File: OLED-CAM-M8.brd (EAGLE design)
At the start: 87.6 x 61 mm, 17 parts, among them J5 U.FL

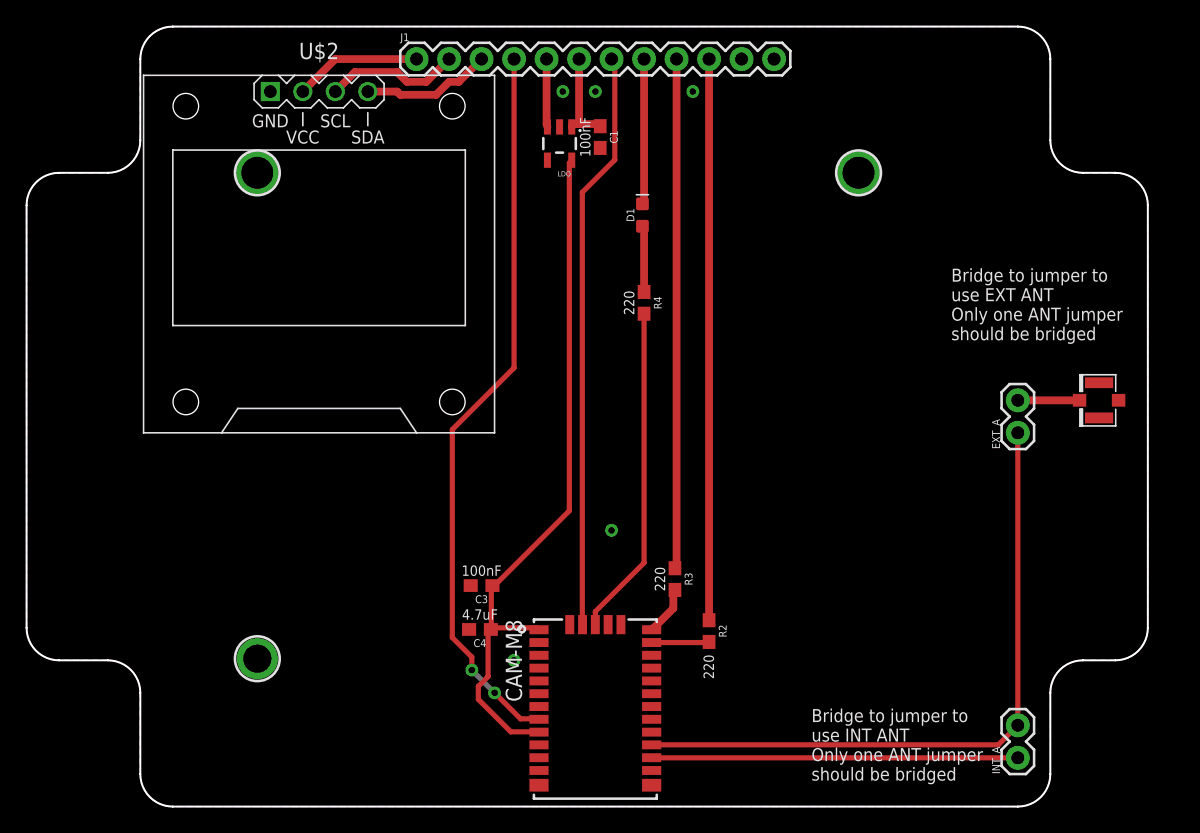
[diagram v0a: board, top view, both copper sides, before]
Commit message: Added GND vias and notes
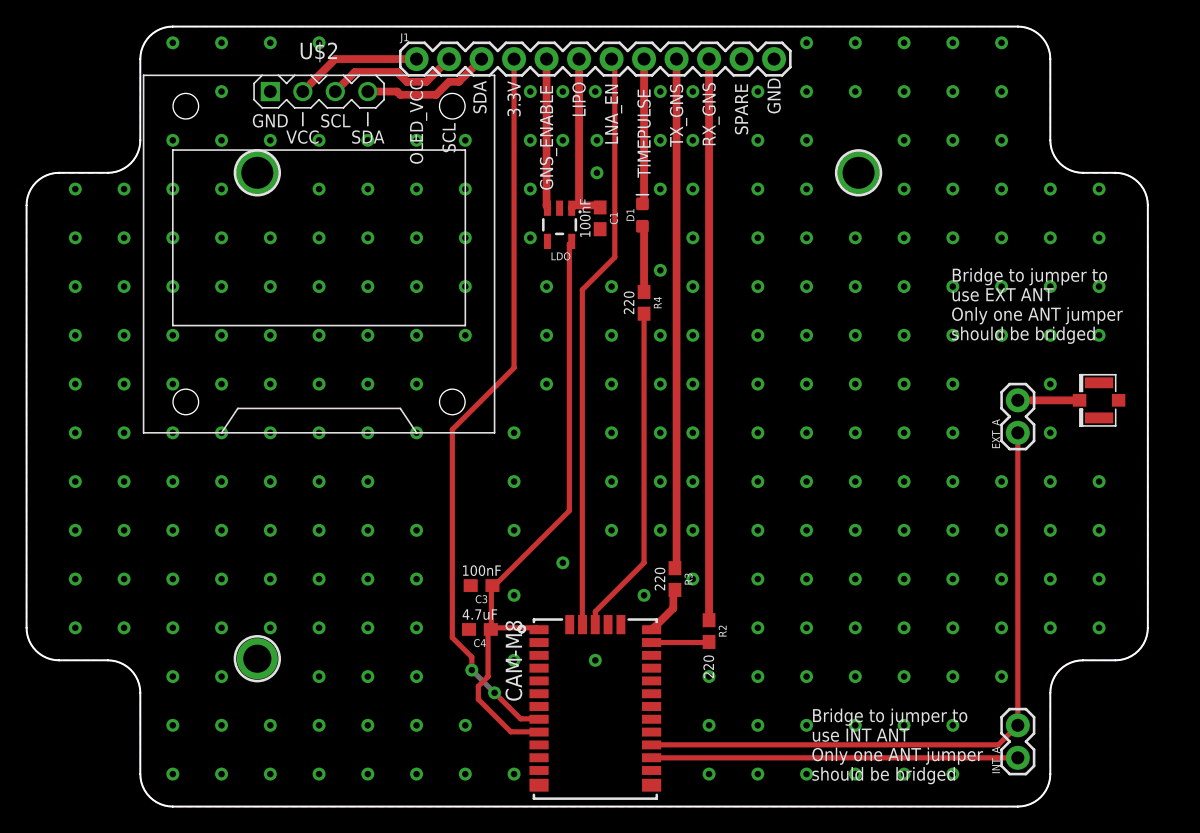
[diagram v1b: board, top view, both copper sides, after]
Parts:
- moved C1 6.35 mm to (44.8, 46.0)
- moved LDO 6.35 mm to (41.7, 45.5)
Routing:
- net GNS_VCC: track 54.9 -> 48.6 mm
- net LIPO: track 7.55 -> 13.9 mm
- net GNS_ENABLE: track 5.31 -> 11.7 mm
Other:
- board text added: "3.3V"
- board text added: "GND"
- board text added: "GNS_ENABLE"
- board text added: "LIPO"
- board text added: "LNA_EN"
- board text added: "OLED_VCC"
- board text added: "RX_GNS"
- board text added: "SCL"
- board text added: "SDA"
- board text added: "SPARE"
- board text added: "TIMEPULSE"
- board text added: "TX_GNS"

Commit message: Added mounting hole
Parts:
- added U$1: MOUNTINGHOLE2.0, microbuilder:MOUNTINGHOLE_2.0_PLATED
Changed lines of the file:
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@@
 <attribute name="VALUE" x="29.21" y="56.388" size="0.6096" layer="27" font="vector" ratio="20"/>
 </element>
+<element name="U$1" library="microbuilder" package="MOUNTINGHOLE_2.0_PLATED" value="MOUNTINGHOLE2.0" x="65.024" y="11.557" smashed="yes"/>
 </elements>
 <signals>
@@
 <via x="60.96" y="13.97" extent="1-16" drill="0.508"/>
 <via x="60.96" y="10.16" extent="1-16" drill="0.508"/>
-<via x="64.77" y="10.16" extent="1-16" drill="0.508"/>
-<via x="64.77" y="13.97" extent="1-16" drill="0.508"/>
 <via x="68.58" y="13.97" extent="1-16" drill="0.508"/>
 <via x="68.58" y="10.16" extent="1-16" drill="0.508"/>

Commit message: Swapped VCC GND
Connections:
- net GND: now also U$2.2; no longer U$2.1
- net OLED_VCC: now also U$2.1; no longer U$2.2
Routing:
- net OLED_VCC: track 9.94 -> 13.4 mm
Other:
- board text added: "v0.4 gregcope@gmail.com OLED-CAM-M8"
- board text removed: "v0.2 gregcope@gmail.com OLED-CAM-M8"
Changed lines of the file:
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@@
 <board>
 <plain>
-<text x="51.181" y="20.447" size="1.778" layer="26">v0.2
+<text x="51.181" y="20.447" size="1.778" layer="26">v0.4
 gregcope@gmail.com
 OLED-CAM-M8</text>
@@
 <contactref element="J5" pad="2"/>
 <contactref element="J5" pad="1"/>
-<contactref element="U$2" pad="1"/>
 <contactref element="J1" pad="12"/>
 <via x="38.1" y="11.43" extent="1-16" drill="0.508"/>
@@
 <via x="76.2" y="55.88" extent="1-16" drill="0.508"/>
 <via x="15.24" y="59.69" extent="1-16" drill="0.508"/>
-<via x="19.05" y="59.69" extent="1-16" drill="0.508"/>
 <via x="11.43" y="59.69" extent="1-16" drill="0.508"/>
 <via x="57.15" y="48.26" extent="1-16" drill="0.508"/>
@@
 <via x="76.2" y="52.07" extent="1-16" drill="0.508"/>
 <via x="76.2" y="48.26" extent="1-16" drill="0.508"/>
-<via x="22.86" y="59.69" extent="1-16" drill="0.508"/>
 <via x="80.01" y="48.26" extent="1-16" drill="0.508"/>
 <via x="52.07" y="55.88" extent="1-16" drill="0.508"/>
@@
 <via x="80.01" y="44.45" extent="1-16" drill="0.508"/>
 <via x="80.01" y="40.64" extent="1-16" drill="0.508"/>
+<contactref element="U$2" pad="2"/>
+<via x="19.05" y="59.69" extent="1-16" drill="0.508"/>
+<via x="22.86" y="59.69" extent="1-16" drill="0.508"/>
+<via x="26.67" y="59.69" extent="1-16" drill="0.508"/>
 </signal>
 <signal name="3.3V" class="2">
@@
 <signal name="OLED_VCC">
 <contactref element="J1" pad="1"/>
-<contactref element="U$2" pad="2"/>
-<wire x1="24.13" y1="58.42" x2="21.59" y2="55.88" width="0.6096" layer="1"/>
-<wire x1="30.48" y1="58.42" x2="24.13" y2="58.42" width="0.6096" layer="1"/>
+<contactref element="U$2" pad="1"/>
+<wire x1="19.05" y1="57.404" x2="19.05" y2="55.88" width="0.6096" layer="16"/>
+<wire x1="19.812" y1="58.166" x2="19.05" y2="57.404" width="0.6096" layer="16"/>
+<wire x1="28.702" y1="58.166" x2="19.812" y2="58.166" width="0.6096" layer="16"/>
+<wire x1="28.956" y1="58.42" x2="28.702" y2="58.166" width="0.6096" layer="16"/>
+<wire x1="30.48" y1="58.42" x2="28.956" y2="58.42" width="0.6096" layer="16"/>
 </signal>
 <signal name="SCL">

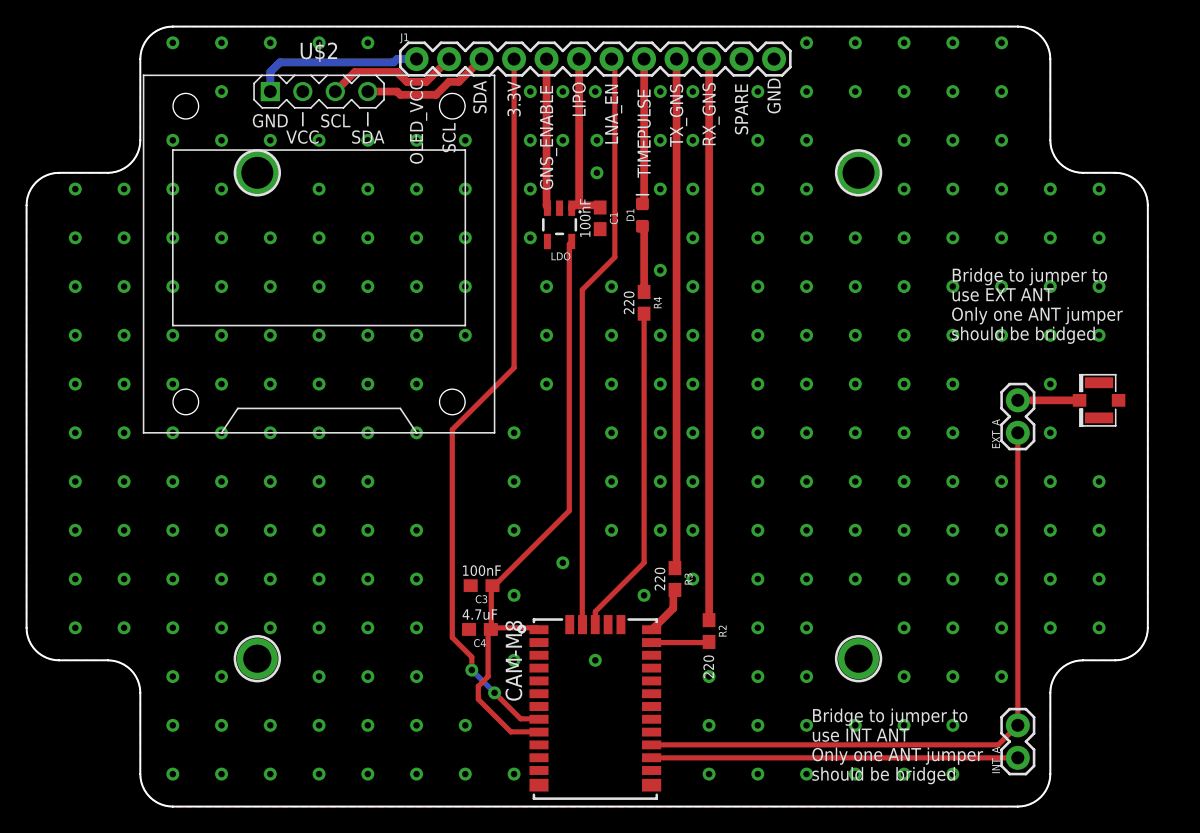
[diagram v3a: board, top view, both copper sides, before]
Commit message: removed mounting hole and moved 100n cap
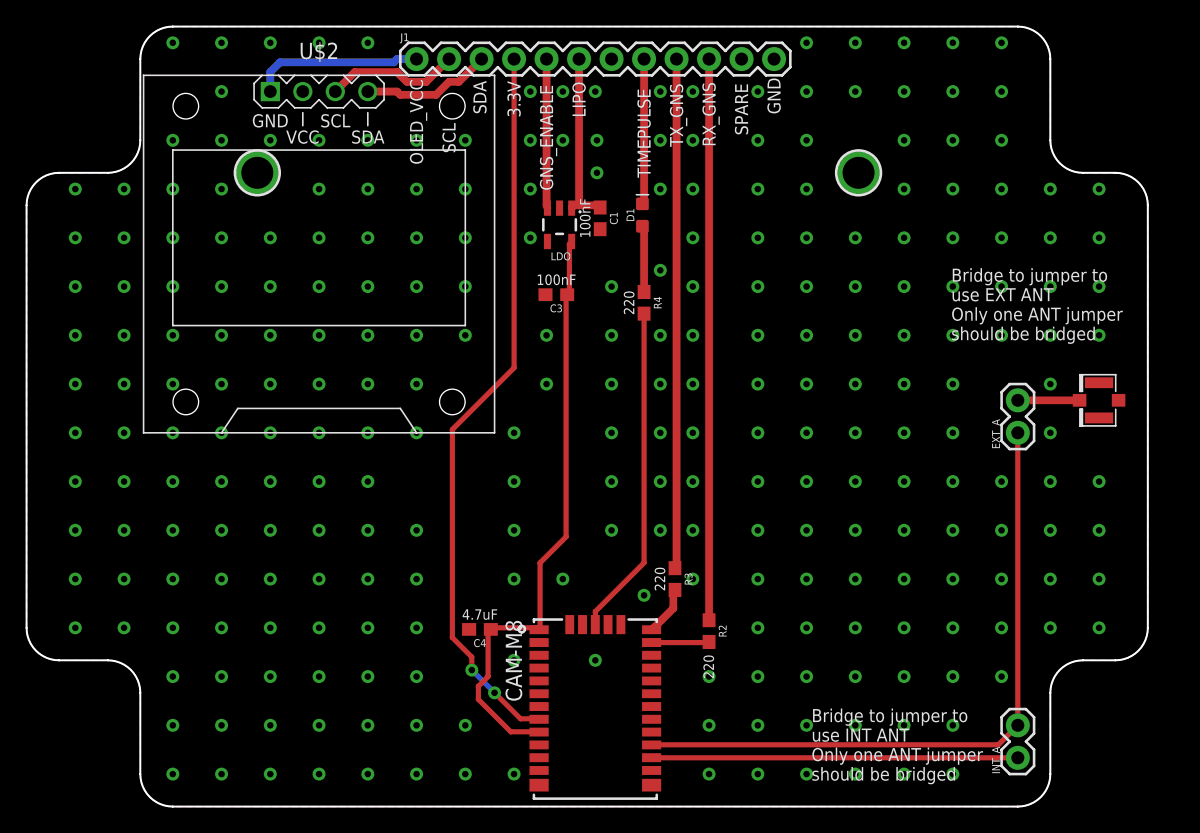
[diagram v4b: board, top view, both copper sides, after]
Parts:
- removed U$1, U$9: MOUNTINGHOLE2.0, microbuilder:MOUNTINGHOLE_2.0_PLATED
- moved C3 23.5 mm to (41.4, 40.0)
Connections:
- removed net LNA_EN: J1.7, U$5.30
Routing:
- net LNA_EN: track 45.4 -> 0.00 mm
- net GNS_VCC: track 48.6 -> 47.3 mm
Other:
- board text removed: "LNA_EN"
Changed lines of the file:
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@@
 <text x="51.308" y="51.562" size="1.016" layer="25" font="vector" ratio="20" rot="R90">TX_GNS</text>
 <text x="48.768" y="49.149" size="1.016" layer="25" font="vector" ratio="20" rot="R90">TIMEPULSE</text>
-<text x="46.228" y="51.689" size="1.016" layer="25" font="vector" ratio="20" rot="R90">LNA_EN</text>
 <text x="43.688" y="53.848" size="1.016" layer="25" font="vector" ratio="20" rot="R90">LIPO</text>
 <text x="41.148" y="48.133" size="1.016" layer="25" font="vector" ratio="20" rot="R90">GNS_ENABLE</text>
@@
 <attribute name="VALUE" x="44.069" y="45.974" size="0.8128" layer="25" font="vector" ratio="20" rot="R270" align="top-center"/>
 </element>
-<element name="C3" library="SparkFun-Capacitors" library_urn="urn:adsk.eagle:library:510" package="0603" package3d_urn="urn:adsk.eagle:package:37414/1" value="100nF" x="35.56" y="17.272" smashed="yes" rot="R180">
-<attribute name="NAME" x="35.56" y="16.51" size="0.6096" layer="25" font="vector" ratio="20" rot="R180" align="bottom-center"/>
-<attribute name="PROD_ID" value="CAP-08604" x="66.04" y="21.082" size="1.778" layer="27" rot="R180" display="off"/>
-<attribute name="VALUE" x="35.56" y="18.034" size="0.8128" layer="25" font="vector" ratio="20" rot="R180" align="top-center"/>
+<element name="C3" library="SparkFun-Capacitors" library_urn="urn:adsk.eagle:library:510" package="0603" package3d_urn="urn:adsk.eagle:package:37414/1" value="100nF" x="41.402" y="40.005" smashed="yes" rot="R180">
+<attribute name="NAME" x="41.402" y="39.243" size="0.6096" layer="25" font="vector" ratio="20" rot="R180" align="bottom-center"/>
+<attribute name="PROD_ID" value="CAP-08604" x="71.882" y="43.815" size="1.778" layer="27" rot="R180" display="off"/>
+<attribute name="VALUE" x="41.402" y="40.767" size="0.8128" layer="25" font="vector" ratio="20" rot="R180" align="top-center"/>
 </element>
 <element name="R2" library="SparkFun-Resistors" library_urn="urn:adsk.eagle:library:532" package="0603" package3d_urn="urn:adsk.eagle:package:39650/1" value="220" x="53.34" y="13.716" smashed="yes" rot="R270">
@@
 <attribute name="VALUE" x="48.768" y="46.228" size="0.6096" layer="27" font="vector" ratio="20" rot="R90" align="top-center"/>
 </element>
-<element name="U$9" library="microbuilder" package="MOUNTINGHOLE_2.0_PLATED" value="MOUNTINGHOLE2.0" x="18.034" y="11.557" smashed="yes"/>
 <element name="J5" library="SparkFun-Connectors" library_urn="urn:adsk.eagle:library:513" package="U.FL" package3d_urn="urn:adsk.eagle:package:38237/1" value="U.FL" x="83.82" y="31.75" smashed="yes" rot="R180">
 <attribute name="PROD_ID" value="CONN-09193" x="83.82" y="31.75" size="1.778" layer="27" rot="R180" display="off"/>
@@
 <attribute name="VALUE" x="29.21" y="56.388" size="0.6096" layer="27" font="vector" ratio="20"/>
 </element>
-<element name="U$1" library="microbuilder" package="MOUNTINGHOLE_2.0_PLATED" value="MOUNTINGHOLE2.0" x="65.024" y="11.557" smashed="yes"/>
 </elements>
 <signals>
@@
 <via x="34.29" y="2.54" extent="1-16" drill="0.508"/>
 <via x="38.1" y="29.21" extent="1-16" drill="0.508"/>
-<via x="45.72" y="40.64" extent="1-16" drill="0.508"/>
 <via x="38.1" y="25.4" extent="1-16" drill="0.508"/>
 <via x="45.72" y="29.21" extent="1-16" drill="0.508"/>
@@
 <via x="30.48" y="17.78" extent="1-16" drill="0.508"/>
 <via x="38.1" y="21.59" extent="1-16" drill="0.508"/>
-<via x="38.1" y="16.51" extent="1-16" drill="0.508"/>
 <via x="3.81" y="40.64" extent="1-16" drill="0.508"/>
 <via x="3.81" y="44.45" extent="1-16" drill="0.508"/>
@@
 <via x="30.48" y="13.97" extent="1-16" drill="0.508"/>
 <via x="30.48" y="10.16" extent="1-16" drill="0.508"/>
-<via x="41.91" y="19.05" extent="1-16" drill="0.508"/>
 <via x="44.45" y="11.43" extent="1-16" drill="0.508"/>
 <via x="7.62" y="48.26" extent="1-16" drill="0.508"/>
@@
 <via x="52.07" y="44.45" extent="1-16" drill="0.508"/>
 <via x="52.07" y="40.64" extent="1-16" drill="0.508"/>
-<via x="40.64" y="40.64" extent="1-16" drill="0.508"/>
-<via x="40.64" y="36.83" extent="1-16" drill="0.508"/>
-<via x="40.64" y="33.02" extent="1-16" drill="0.508"/>
 <via x="49.53" y="25.4" extent="1-16" drill="0.508"/>
 <via x="49.53" y="21.59" extent="1-16" drill="0.508"/>
@@
 <via x="22.86" y="59.69" extent="1-16" drill="0.508"/>
 <via x="26.67" y="59.69" extent="1-16" drill="0.508"/>
+<via x="19.05" y="10.16" extent="1-16" drill="0.508"/>
+<via x="64.77" y="10.16" extent="1-16" drill="0.508"/>
+<via x="64.77" y="13.97" extent="1-16" drill="0.508"/>
+<via x="38.1" y="17.78" extent="1-16" drill="0.508"/>
+<via x="41.91" y="17.78" extent="1-16" drill="0.508"/>
+<via x="40.64" y="33.02" extent="1-16" drill="0.508"/>
+<via x="40.64" y="36.83" extent="1-16" drill="0.508"/>
+<via x="45.72" y="40.64" extent="1-16" drill="0.508"/>
 </signal>
 <signal name="3.3V" class="2">
@@
 <contactref element="U$5" pad="9"/>
 <contactref element="U$5" pad="1"/>
-<wire x1="36.322" y1="17.272" x2="36.322" y2="13.97" width="0.4064" layer="1"/>
-<wire x1="36.322" y1="17.272" x2="36.41" y2="17.272" width="0.4064" layer="1"/>
-<wire x1="42.418" y1="23.114" x2="42.418" y2="43.942" width="0.4064" layer="1"/>
-<wire x1="36.576" y1="17.272" x2="42.418" y2="23.114" width="0.4064" layer="1"/>
-<wire x1="42.418" y1="43.942" x2="42.606" y2="44.1659" width="0.4064" layer="1"/>
-<wire x1="36.576" y1="17.272" x2="36.41" y2="17.272" width="0.4064" layer="1"/>
+<wire x1="42.164" y1="40.005" x2="42.252" y2="40.005" width="0.4064" layer="1"/>
+<wire x1="42.418" y1="40.005" x2="42.252" y2="40.005" width="0.4064" layer="1"/>
 <wire x1="37.846" y1="5.842" x2="39.878" y2="5.842" width="0.4064" layer="1"/>
 <wire x1="35.306" y1="8.382" x2="37.846" y2="5.842" width="0.4064" layer="1"/>
@@
 <wire x1="39.878" y1="13.97" x2="40.05" y2="13.82" width="0.4064" layer="1"/>
 <wire x1="36.322" y1="13.97" x2="36.283" y2="13.843" width="0.4064" layer="1"/>
+<wire x1="42.418" y1="43.942" x2="42.418" y2="40.132" width="0.4064" layer="1"/>
+<wire x1="42.418" y1="40.132" x2="42.252" y2="40.005" width="0.4064" layer="1"/>
+<wire x1="42.418" y1="43.942" x2="42.606" y2="44.1659" width="0.4064" layer="1"/>
+<wire x1="42.164" y1="21.082" x2="42.164" y2="39.878" width="0.4064" layer="1"/>
+<wire x1="40.132" y1="19.05" x2="42.164" y2="21.082" width="0.4064" layer="1"/>
+<wire x1="40.132" y1="13.97" x2="40.132" y2="19.05" width="0.4064" layer="1"/>
+<wire x1="42.164" y1="39.878" x2="42.252" y2="40.005" width="0.4064" layer="1"/>
+<wire x1="40.132" y1="13.97" x2="40.05" y2="13.82" width="0.4064" layer="1"/>
 </signal>
 <signal name="GNS_ENABLE">
@@
 <wire x1="48.26" y1="47.244" x2="48.133" y2="47.105" width="0.6096" layer="1"/>
 </signal>
-<signal name="LNA_EN" class="2">
-<contactref element="U$5" pad="30"/>
-<contactref element="J1" pad="7"/>
-<wire x1="45.974" y1="58.166" x2="45.974" y2="42.926" width="0.4064" layer="1"/>
-<wire x1="45.72" y1="58.42" x2="45.974" y2="58.166" width="0.4064" layer="1"/>
-<wire x1="43.434" y1="40.386" x2="43.434" y2="14.224" width="0.4064" layer="1"/>
-<wire x1="45.974" y1="42.926" x2="43.434" y2="40.386" width="0.4064" layer="1"/>
-<wire x1="43.434" y1="14.224" x2="43.45" y2="14.22" width="0.4064" layer="1"/>
-</signal>
 <signal name="OLED_VCC">
